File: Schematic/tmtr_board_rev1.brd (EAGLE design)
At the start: 50 x 80 mm, 43 parts, among them J1 22-23-2021, J2 POWER_JACKPTH_LOCK, J4 22-23-2021, J6 AVR_SPI_PROG, J7 22-23-2021, J8 22-23-2021, U2 LD117AS12TR, U3 MEGA8-AI, U4 MAX31855, U5 MAX31855

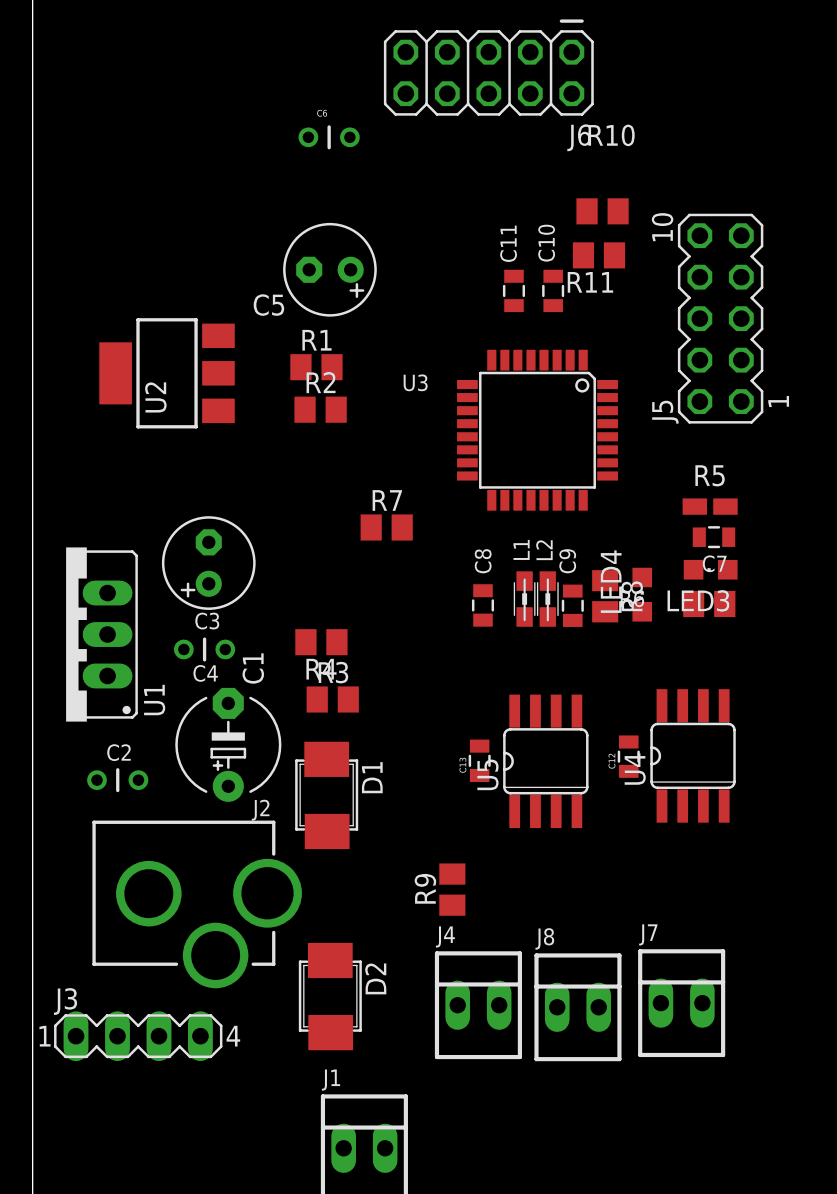
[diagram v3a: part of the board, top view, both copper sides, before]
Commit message: 
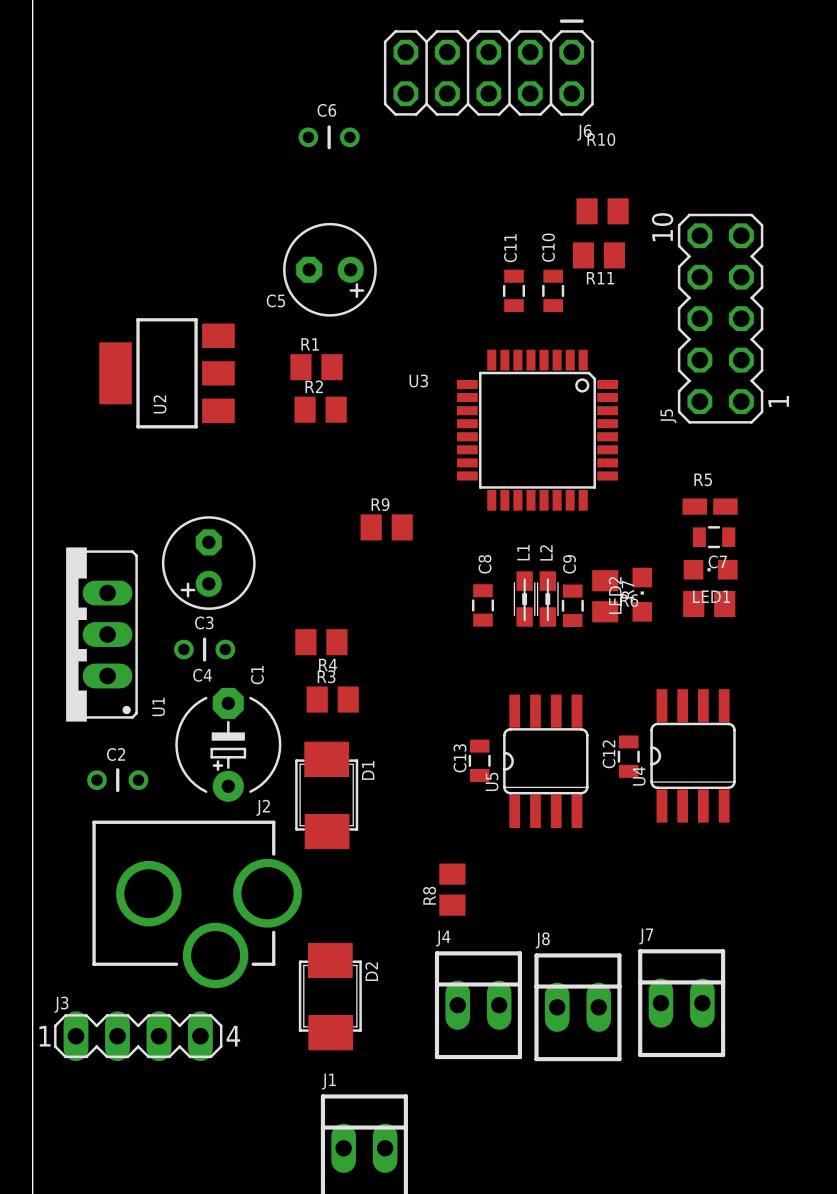
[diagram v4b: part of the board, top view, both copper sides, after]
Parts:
- moved R9 22.5 mm to (21.7, 46.3), turned to 0 degrees
- moved R8 20.3 mm to (25.7, 24.1), turned to 90 degrees
- moved R7 14.0 mm to (35.1, 42.1), turned to 270 degrees
- renumbered LED3 to LED1, LED4 to LED2
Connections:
- net 5V: now also R7.1; no longer R9.1
- net N$10: now also R7.2; no longer R8.2
- net N$3: now also R9.2; no longer R7.2
- net N$9: now also R8.2; no longer R9.2
- net VIN_SENSE: now also R9.1; no longer R7.1
